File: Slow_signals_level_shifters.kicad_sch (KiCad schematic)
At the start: 34 parts, among them IC3 TCA9406DCUR, IC4 TCA9406DCUR, IC5 TCA9406DCUR, IC7 SN74AVC1T45DCKT, U3 SN74AVCH16T245_DGV_48

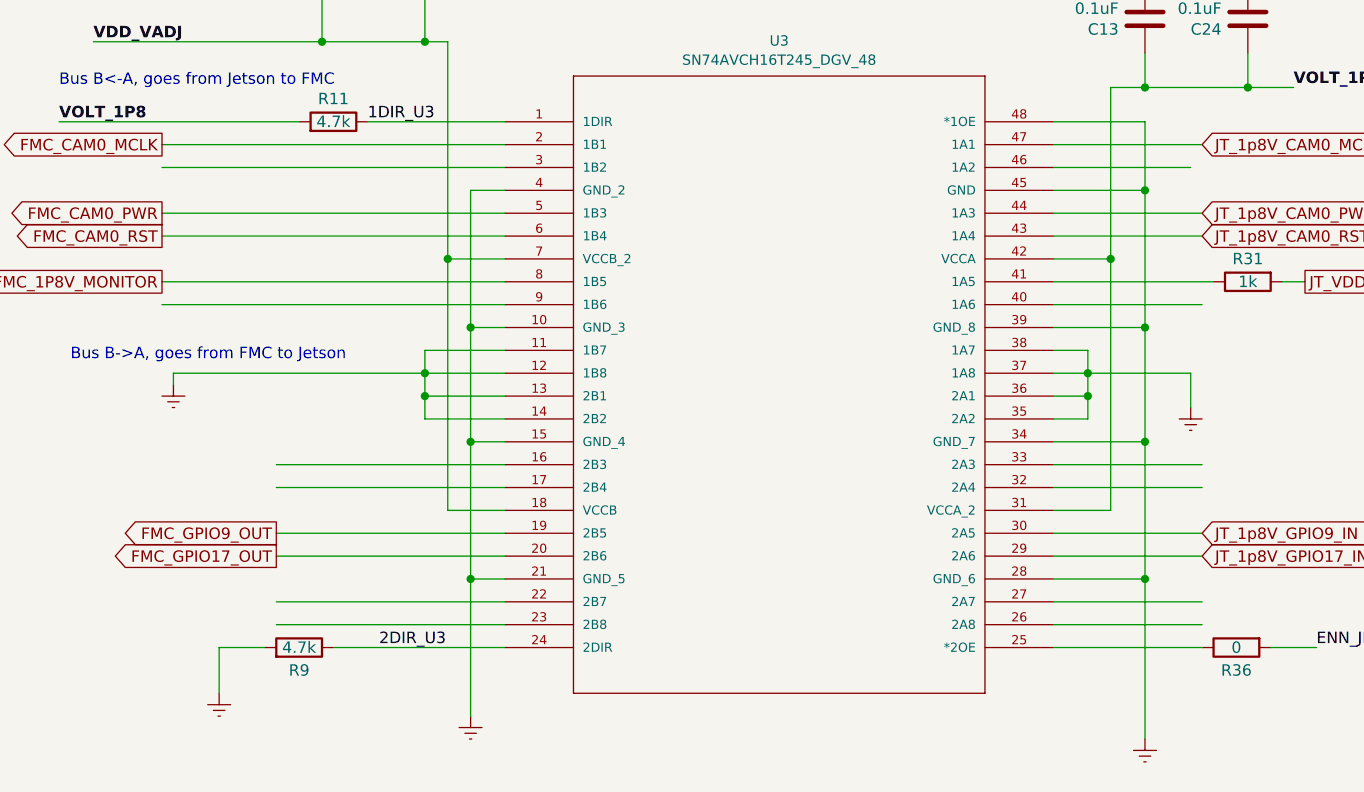
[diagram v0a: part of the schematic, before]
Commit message: DRC, ERC OK
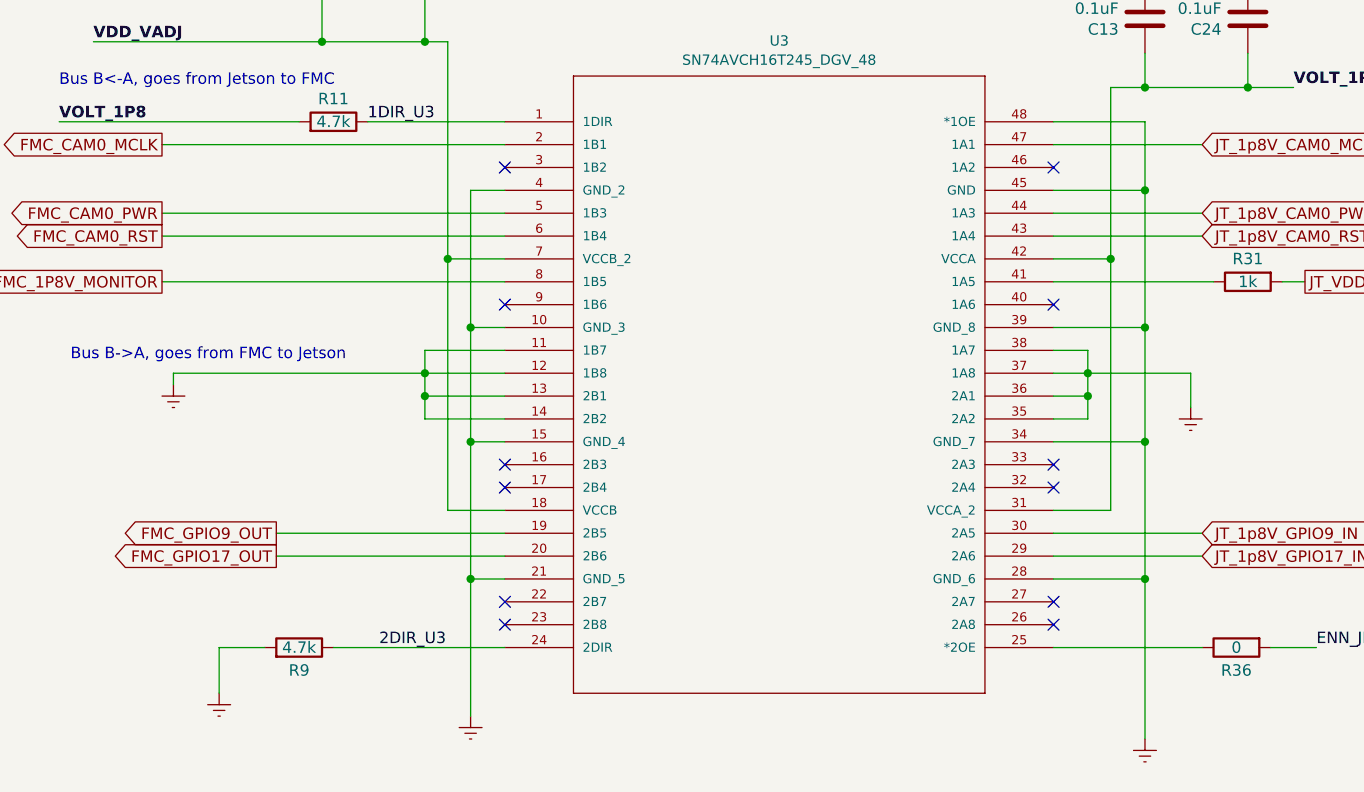
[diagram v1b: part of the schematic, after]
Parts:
- IC3, IC4, IC5: footprint FMC_MIPI_v2_sym:SOP50P310X90-8N -> SOP50P310X90-8N
- IC7: footprint FMC_MIPI_v2_sym:SOT65P210X110-6N -> SOT65P210X110-6N
- R11, R12, R13, R14, R15, R19, R20, R21, R22, R23, R24, R25, R26, R31, R35, R36, R9: symbol FMC_MIPI_v2-rescue:R-Device -> FMC_MIPI_v2:R
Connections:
- removed net Earth: C10.2, C11.2, C12.2, C13.2, C24.2, C32.2, C33.2, C34.2, C35.2, C40.1, C41.1, C9.2, IC3.2 (GND), IC4.2 (GND), IC5.2 (GND), IC7.2 (GND), R9.2, U3.10 (GND_3), U3.11 (1B7), U3.12 (1B8), U3.13 (2B1), U3.14 (2B2), U3.15 (GND_4), U3.21 (GND_5), U3.28 (GND_6), U3.34 (GND_7), U3.35 (2A2), U3.36 (2A1), U3.37 (1A8), U3.38 (1A7), U3.39 (GND_8), U3.4 (GND_2), U3.45 (GND), U3.48 (*1OE)
- new net: C10.2, C9.2
- new net: C13.2, C24.2
- new net: U3.10 (GND_3), U3.15 (GND_4), U3.21 (GND_5), U3.4 (GND_2)
- new net: U3.11 (1B7), U3.12 (1B8), U3.13 (2B1), U3.14 (2B2)
- new net: U3.28 (GND_6), U3.34 (GND_7), U3.39 (GND_8), U3.45 (GND), U3.48 (*1OE)
- new net: U3.35 (2A2), U3.36 (2A1), U3.37 (1A8), U3.38 (1A7)
- no-connect marks 0 -> 12

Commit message: All warnings fixed
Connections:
- net Earth: now reaches IC3.2 (GND)
- net Earth: now also C10.2, C11.2, C12.2, C13.2, C24.2, C32.2, C33.2, C34.2, C35.2, C40.1, C41.1, C9.2, IC4.2 (GND), IC5.2 (GND), IC7.2 (GND), R9.2, U3.10 (GND_3), U3.11 (1B7), U3.12 (1B8), U3.13 (2B1), U3.14 (2B2), U3.15 (GND_4), U3.21 (GND_5), U3.28 (GND_6), U3.34 (GND_7), U3.35 (2A2), U3.36 (2A1), U3.37 (1A8), U3.38 (1A7), U3.39 (GND_8), U3.4 (GND_2), U3.45 (GND), U3.48 (*1OE)

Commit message: JLCPCB BOM OK
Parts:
- C10, C11, C12, C24, C32, C33, C34, C35, C40, C41, C9: LCSC (none) -> C1525
- IC3: LCSC (none) -> C840107
- IC7: LCSC (none) -> NeedToAsk
- R11, R9: LCSC (none) -> C17673
- R12, R13, R14, R15, R19, R20, R21, R22, R23, R24, R25, R26, R36: LCSC (none) -> C17477; Part Number RC0805JR-070RL -> 0805W8F0000T5E
- R31: value 1k -> 2.2k; LCSC (none) -> C17520; Part Number CRCW08051K00FKEAC -> (none)
- U3: value SN74AVCH16T245_DGV_48 -> SN74AVCH16T245GR; footprint FMC_MIPI_v2_sym:DGV48 -> FMC_MIPI_v2_sym:SOP50P810X120-48N; LCSC (none) -> C181413

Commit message: All DRC, ERC and BOM are good
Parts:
- U3: footprint FMC_MIPI_v2_sym:SOP50P810X120-48N -> SOP50P810X120-48N; symbol FMC_MIPI_v2:SN74AVCH16T245_DGV_48 -> FMC_MIPI_v2:SN74AVCH16T245GR; Height (none) -> 1.2; Manufacturer_Name (none) -> Texas Instruments; Manufacturer_Part_Number (none) -> SN74AVCH16T245GR; Mouser Part Number (none) -> 595-SN74AVCH16T245GR; Mouser Price/Stock (none) -> https://www.mouser.co.uk/ProductDetail/Texas-Instruments/SN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
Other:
- moved on the sheet: C13, C24, R31, R36

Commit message: Generated BOM, before Gerbers generation
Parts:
- IC7: LCSC NeedToAsk -> C2677669
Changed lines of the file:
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@@
       (effects (font (size 1.27 1.27)) (justify left) hide)
     )
-    (property "LCSC" "NeedToAsk" (id 10) (at 139.7 156.21 0)
+    (property "LCSC" "C2677669" (id 10) (at 139.7 156.21 0)
       (effects (font (size 1.27 1.27)) hide)
     )
